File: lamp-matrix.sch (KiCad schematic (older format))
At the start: 38 parts

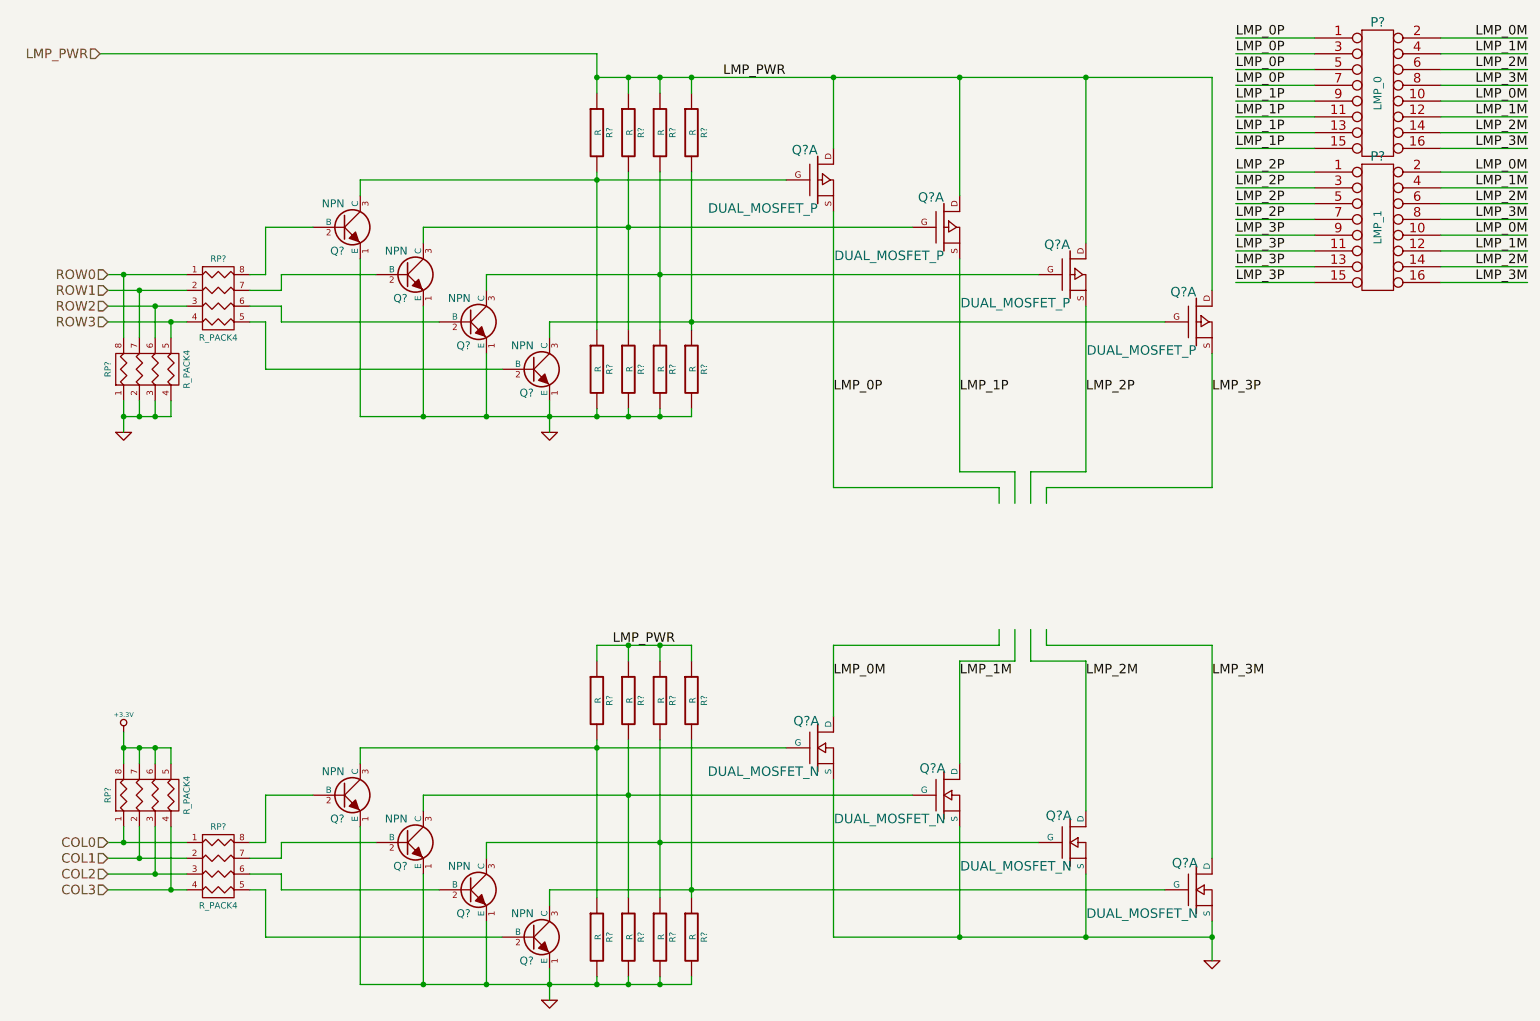
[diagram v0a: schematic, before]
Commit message: changed the controller adding some shift registers
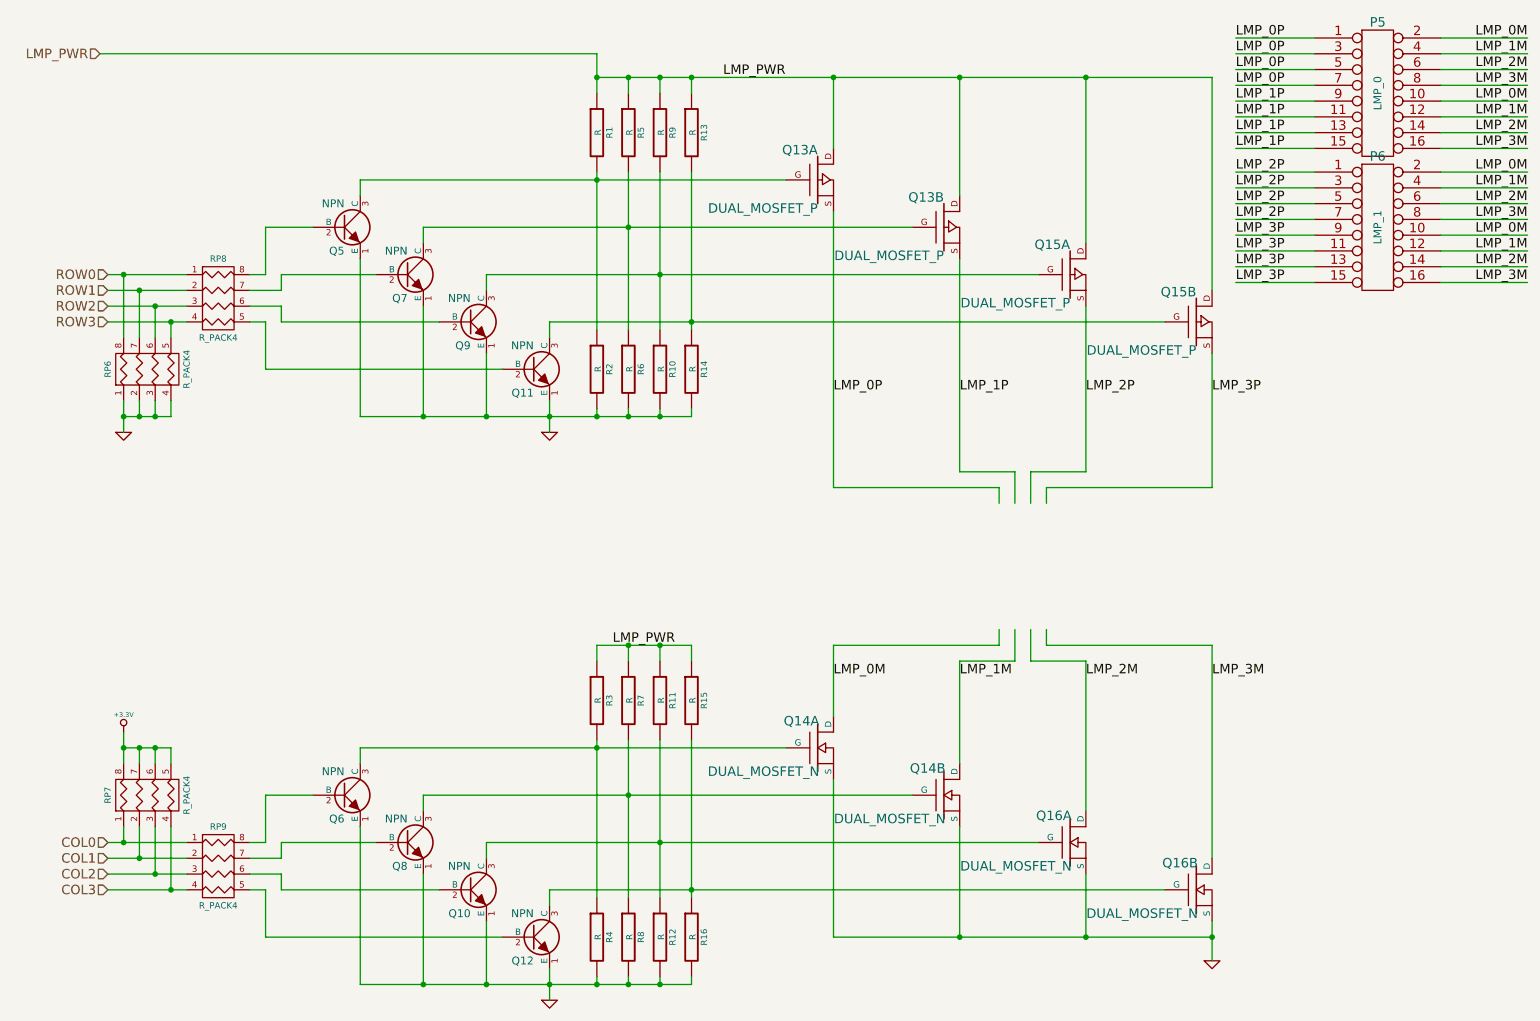
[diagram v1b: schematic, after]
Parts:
- gave numbers to parts that had none: 34
